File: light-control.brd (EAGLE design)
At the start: 100 x 80 mm, 28 parts, among them IC1 ULN2003AN, IC2 MEGA8-P, K1 JS-M1-12V-5, K2 JS-M1-12V-5, K3 JS-M1-12V-5, K4 JS-M1-12V-5

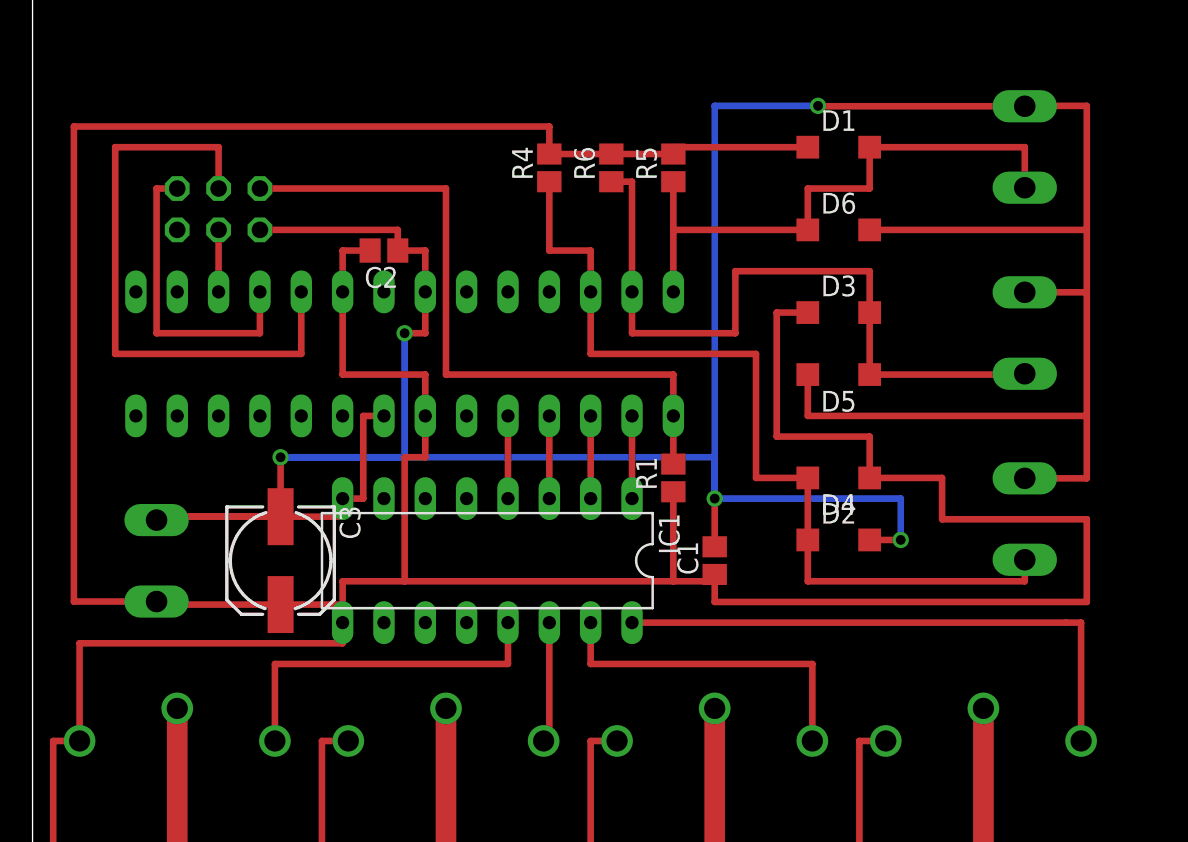
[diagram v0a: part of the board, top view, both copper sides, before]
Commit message: Moved to TQFP
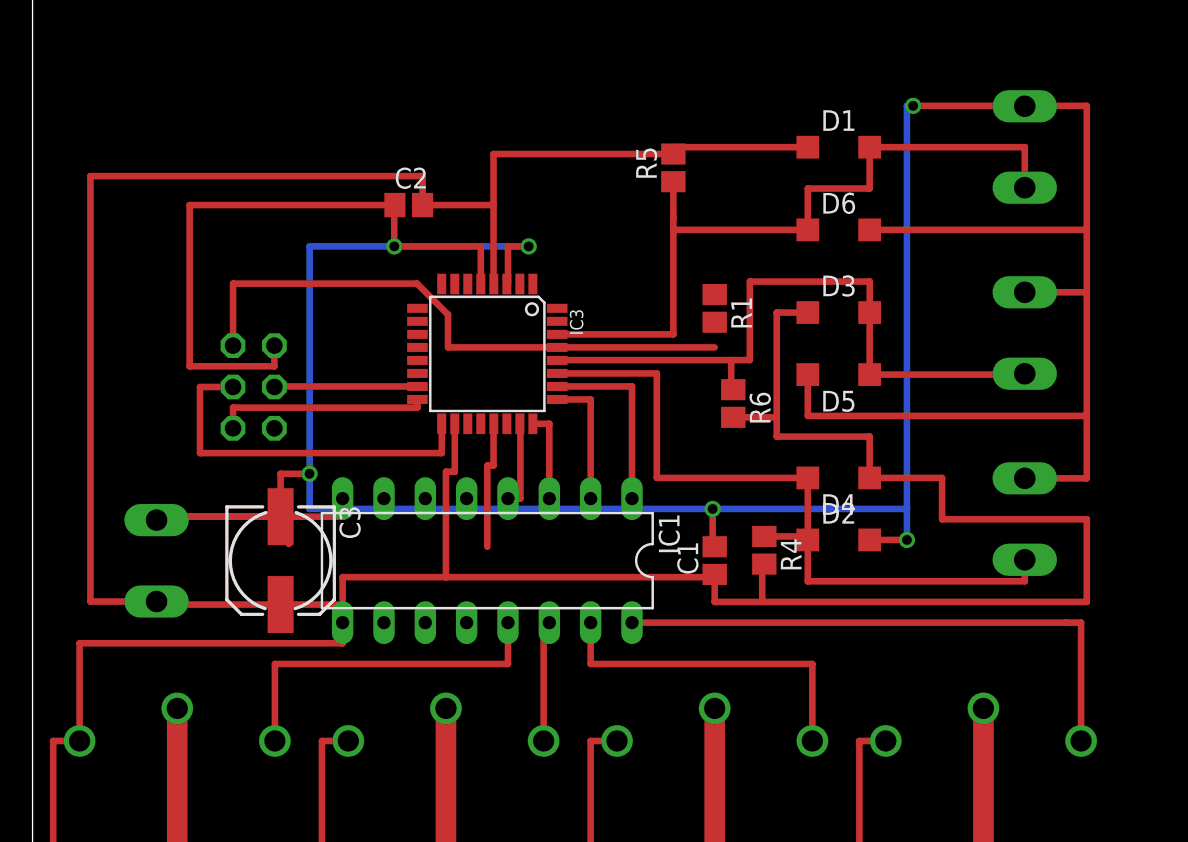
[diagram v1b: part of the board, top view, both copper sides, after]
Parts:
- removed IC2: MEGA8-P, atmel:DIL28-3
- added IC3: MEGA8-AI, atmel:TQFP32-08
- moved R4 27.0 mm to (45.0, 42.5), turned to 270 degrees
- moved R6 16.3 mm to (43.1, 51.6), turned to 270 degrees
- moved JP1 11.1 mm to (13.6, 52.6), turned to 90 degrees
- moved R1 10.7 mm to (41.9, 57.4), turned to 270 degrees
- moved C2 3.18 mm to (23.1, 63.8), turned to 0 degrees
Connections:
- removed net N$1: IC1.1, IC2.2
- removed net N$21: D2.C, D4.A, IC2.26, R4.1, X1.2
- removed net N$22: D3.A, D5.C, IC2.27, R6.1, X2.2
- removed net N$23: D1.A, D6.C, IC2.28, R5.1, X3.2
- removed net N$6: IC1.2, IC2.3
- removed net N$7: IC1.3, IC2.4
- removed net N$8: IC1.4, IC2.5
- new net BUT1: D2.C, D4.A, IC3.27, R4.1, X1.2
- new net BUT2: D3.A, D5.C, IC3.28, R6.1, X2.2
- new net BUT3: D1.A, D6.C, IC3.30, R5.1, X3.2
- new net CHAN1: IC1.1, IC3.26
- new net CHAN2: IC1.2, IC3.25
- new net CHAN3: IC1.3, IC3.24
- new net CHAN4: IC1.4, IC3.23
- new net VCC: IC3.6
- net +5V: now also IC3.18, IC3.4; no longer C1.1, IC2.20, IC2.7
- net GND: now also IC3.21, IC3.3, IC3.5; no longer IC2.22, IC2.8
- net N$2: now also IC3.16; no longer IC2.18
- net N$3: now also IC3.17; no longer IC2.19
- net N$4: now also IC3.15; no longer IC2.17
- net N$5: now also C1.1, IC3.29; no longer IC2.1
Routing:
- net N$21: track 55.1 -> 0.00 mm
- net BUT1: track 0.00 -> 46.0 mm
- net BUT3: track 0.00 -> 45.7 mm
- net N$22: track 44.9 -> 0.00 mm
- net BUT2: track 0.00 -> 41.3 mm
- net N$23: track 35.9 -> 0.00 mm
- net GND: track 222.0 -> 247.5 mm, vias 5 -> 6
- net +5V: track 415.1 -> 399.0 mm
- net N$3: track 36.8 -> 22.8 mm
- net CHAN1: track 0.00 -> 11.5 mm
- net CHAN2: track 0.00 -> 8.15 mm
- net N$5: track 42.3 -> 36.2 mm
- net N$2: track 19.0 -> 13.1 mm
- net CHAN3: track 0.00 -> 5.61 mm
- net CHAN4: track 0.00 -> 5.39 mm
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
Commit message: Some optimizations to board
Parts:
- moved C1 36.0 mm to (7.04, 50.8), turned to 270 degrees
- moved R1 35.7 mm to (6.30, 55.2), turned to 0 degrees
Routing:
- net GND: track 247.5 -> 208.4 mm

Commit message: Some optimizations on board
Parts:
- moved D4 6.47 mm to (43.1, 47.5)
- moved D2 5.34 mm to (53.1, 47.2), turned to 90 degrees
- moved R4 4.42 mm to (40.6, 43.5)
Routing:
- net GND: track 208.4 -> 190.4 mm, vias 6 -> 4
- net BUT1: track 46.0 -> 42.3 mm
- net BUT2: track 41.3 -> 42.3 mm

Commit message: Added initial firmware
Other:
- board size 100 x 80 mm -> 67.6 x 73.8 mm
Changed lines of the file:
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@@
 <?xml version="1.0" encoding="utf-8"?>
 <!DOCTYPE eagle SYSTEM "eagle.dtd">
-<eagle version="7.1.0">
+<eagle version="7.2.0">
 <drawing>
 <settings>
@@
 <setting verticaltext="up"/>
 </settings>
-<grid distance="0.001" unitdist="inch" unit="inch" style="lines" multiple="1" display="no" altdistance="0.0005" altunitdist="inch" altunit="inch"/>
+<grid distance="0.001" unitdist="inch" unit="mm" style="lines" multiple="1" display="no" altdistance="0.0005" altunitdist="inch" altunit="inch"/>
 <layers>
 <layer number="1" name="Top" color="4" fill="1" visible="yes" active="yes"/>
@@
 <layer number="31" name="tCream" color="7" fill="4" visible="no" active="yes"/>
 <layer number="32" name="bCream" color="7" fill="5" visible="no" active="yes"/>
-<layer number="33" name="tFinish" color="6" fill="3" visible="no" active="yes"/>
-<layer number="34" name="bFinish" color="6" fill="6" visible="no" active="yes"/>
+<layer number="33" name="tFinish" color="6" fill="3" visible="yes" active="yes"/>
+<layer number="34" name="bFinish" color="6" fill="6" visible="yes" active="yes"/>
 <layer number="35" name="tGlue" color="7" fill="4" visible="no" active="yes"/>
 <layer number="36" name="bGlue" color="7" fill="5" visible="no" active="yes"/>
-<layer number="37" name="tTest" color="7" fill="1" visible="no" active="yes"/>
-<layer number="38" name="bTest" color="7" fill="1" visible="no" active="yes"/>
+<layer number="37" name="tTest" color="7" fill="1" visible="yes" active="yes"/>
+<layer number="38" name="bTest" color="7" fill="1" visible="yes" active="yes"/>
 <layer number="39" name="tKeepout" color="4" fill="11" visible="yes" active="yes"/>
 <layer number="40" name="bKeepout" color="1" fill="11" visible="yes" active="yes"/>
@@
 <layer number="43" name="vRestrict" color="2" fill="10" visible="yes" active="yes"/>
 <layer number="44" name="Drills" color="7" fill="1" visible="no" active="yes"/>
-<layer number="45" name="Holes" color="7" fill="1" visible="no" active="yes"/>
-<layer number="46" name="Milling" color="3" fill="1" visible="no" active="yes"/>
-<layer number="47" name="Measures" color="7" fill="1" visible="no" active="yes"/>
+<layer number="45" name="Holes" color="7" fill="1" visible="yes" active="yes"/>
+<layer number="46" name="Milling" color="3" fill="1" visible="yes" active="yes"/>
+<layer number="47" name="Measures" color="7" fill="1" visible="yes" active="yes"/>
 <layer number="48" name="Document" color="7" fill="1" visible="yes" active="yes"/>
 <layer number="49" name="Reference" color="7" fill="1" visible="yes" active="yes"/>
@@
 <layer number="98" name="Guide" color="6" fill="1" visible="no" active="no"/>
 <layer number="99" name="SpiceOrder" color="5" fill="1" visible="no" active="no"/>
+<layer number="116" name="centerDrill" color="7" fill="1" visible="no" active="yes"/>
 </layers>
 <board>
 <plain>
-<wire x1="0" y1="0" x2="100" y2="0" width="0" layer="20"/>
-<wire x1="100" y1="0" x2="100" y2="80" width="0" layer="20"/>
-<wire x1="100" y1="80" x2="0" y2="80" width="0" layer="20"/>
-<wire x1="0" y1="80" x2="0" y2="0" width="0" layer="20"/>
+<wire x1="0" y1="0" x2="67.6404" y2="0" width="0" layer="20"/>
+<wire x1="67.6404" y1="0" x2="67.6404" y2="73.777" width="0" layer="20"/>
+<wire x1="67.6404" y1="73.777" x2="0" y2="73.777" width="0" layer="20"/>
+<wire x1="0" y1="73.777" x2="0" y2="0" width="0" layer="20"/>
+<circle x="36.83" y="45.72" radius="0.303" width="0.306" layer="116"/>
+<circle x="34.29" y="45.72" radius="0.303" width="0.306" layer="116"/>
+<circle x="31.75" y="45.72" radius="0.303" width="0.306" layer="116"/>
+<circle x="29.21" y="45.72" radius="0.303" width="0.306" layer="116"/>
+<circle x="26.67" y="45.72" radius="0.303" width="0.306" layer="116"/>
+<circle x="24.13" y="45.72" radius="0.303" width="0.306" layer="116"/>
+<circle x="21.59" y="45.72" radius="0.303" width="0.306" layer="116"/>
+<circle x="19.05" y="45.72" radius="0.303" width="0.306" layer="116"/>
+<circle x="19.05" y="38.1" radius="0.303" width="0.306" layer="116"/>
+<circle x="21.59" y="38.1" radius="0.303" width="0.306" layer="116"/>
+<circle x="24.13" y="38.1" radius="0.303" width="0.306" layer="116"/>
+<circle x="26.67" y="38.1" radius="0.303" width="0.306" layer="116"/>
+<circle x="29.21" y="38.1" radius="0.303" width="0.306" layer="116"/>
+<circle x="31.75" y="38.1" radius="0.303" width="0.306" layer="116"/>
+<circle x="34.29" y="38.1" radius="0.303" width="0.306" layer="116"/>
+<circle x="36.83" y="38.1" radius="0.303" width="0.306" layer="116"/>
+<circle x="12.319" y="50.038" radius="0.354" width="0.408" layer="116"/>
+<circle x="14.859" y="50.038" radius="0.354" width="0.408" layer="116"/>
+<circle x="12.319" y="52.578" radius="0.354" width="0.408" layer="116"/>
+<circle x="14.859" y="52.578" radius="0.354" width="0.408" layer="116"/>
+<circle x="12.319" y="55.118" radius="0.354" width="0.408" layer="116"/>
+<circle x="14.859" y="55.118" radius="0.354" width="0.408" layer="116"/>
+<circle x="64.42" y="30.83" radius="0.425" width="0.55" layer="116"/>
+<circle x="52.42" y="30.83" radius="0.425" width="0.55" layer="116"/>
+<circle x="58.42" y="32.83" radius="0.425" width="0.55" layer="116"/>
+<circle x="52.42" y="18.63" radius="0.425" width="0.55" layer="116"/>
+<circle x="64.42" y="18.63" radius="0.425" width="0.55" layer="116"/>
+<circle x="47.91" y="30.83" radius="0.425" width="0.55" layer="116"/>
+<circle x="35.91" y="30.83" radius="0.425" width="0.55" layer="116"/>
+<circle x="41.91" y="32.83" radius="0.425" width="0.55" layer="116"/>
+<circle x="35.91" y="18.63" radius="0.425" width="0.55" layer="116"/>
+<circle x="47.91" y="18.63" radius="0.425" width="0.55" layer="116"/>
+<circle x="31.4" y="30.83" radius="0.425" width="0.55" layer="116"/>
+<circle x="19.4" y="30.83" radius="0.425" width="0.55" layer="116"/>
+<circle x="25.4" y="32.83" radius="0.425" width="0.55" layer="116"/>
+<circle x="19.4" y="18.63" radius="0.425" width="0.55" layer="116"/>
+<circle x="31.4" y="18.63" radius="0.425" width="0.55" layer="116"/>
+<circle x="14.89" y="30.83" radius="0.425" width="0.55" layer="116"/>
+<circle x="2.89" y="30.83" radius="0.425" width="0.55" layer="116"/>
+<circle x="8.89" y="32.83" radius="0.425" width="0.55" layer="116"/>
+<circle x="2.89" y="18.63" radius="0.425" width="0.55" layer="116"/>
+<circle x="14.89" y="18.63" radius="0.425" width="0.55" layer="116"/>
+<circle x="7.62" y="39.395" radius="0.43" width="0.56" layer="116"/>
+<circle x="7.62" y="44.399" radius="0.43" width="0.56" layer="116"/>
+<circle x="60.96" y="46.965" radius="0.43" width="0.56" layer="116"/>
+<circle x="60.96" y="41.961" radius="0.43" width="0.56" layer="116"/>
+<circle x="60.96" y="58.395" radius="0.43" width="0.56" layer="116"/>
+<circle x="60.96" y="53.391" radius="0.43" width="0.56" layer="116"/>
+<circle x="60.96" y="69.825" radius="0.43" width="0.56" layer="116"/>
+<circle x="60.96" y="64.821" radius="0.43" width="0.56" layer="116"/>
+<circle x="63.424" y="6.35" radius="0.43" width="0.56" layer="116"/>
+<circle x="58.42" y="6.35" radius="0.43" width="0.56" layer="116"/>
+<circle x="53.416" y="6.35" radius="0.43" width="0.56" layer="116"/>
+<circle x="46.914" y="6.35" radius="0.43" width="0.56" layer="116"/>
+<circle x="41.91" y="6.35" radius="0.43" width="0.56" layer="116"/>
+<circle x="36.906" y="6.35" radius="0.43" width="0.56" layer="116"/>
+<circle x="30.404" y="6.35" radius="0.43" width="0.56" layer="116"/>
+<circle x="25.4" y="6.35" radius="0.43" width="0.56" layer="116"/>
+<circle x="20.396" y="6.35" radius="0.43" width="0.56" layer="116"/>
+<circle x="15.164" y="6.35" radius="0.43" width="0.56" layer="116"/>
+<circle x="10.16" y="6.35" radius="0.43" width="0.56" layer="116"/>
+<circle x="5.156" y="6.35" radius="0.43" width="0.56" layer="116"/>
+<circle x="28.346" y="48.057" radius="0.25" width="0.2" layer="116"/>
+<circle x="17.145" y="46.939" radius="0.25" width="0.2" layer="116"/>
+<circle x="31.191" y="61.849" radius="0.25" width="0.2" layer="116"/>
+<circle x="47.65" y="48.997" radius="0.25" width="0.2" layer="116"/>
 </plain>
 <attributes>

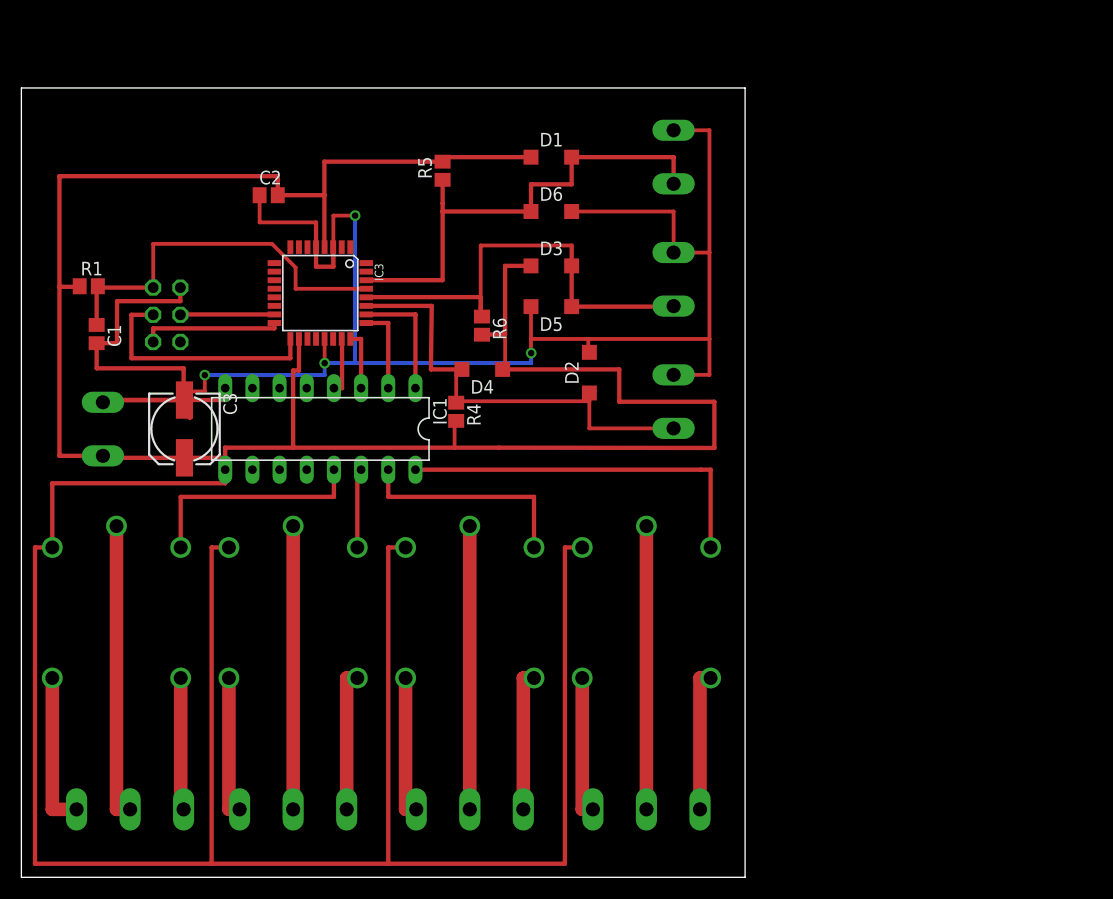
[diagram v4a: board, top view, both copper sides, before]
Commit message: Fixed schematic
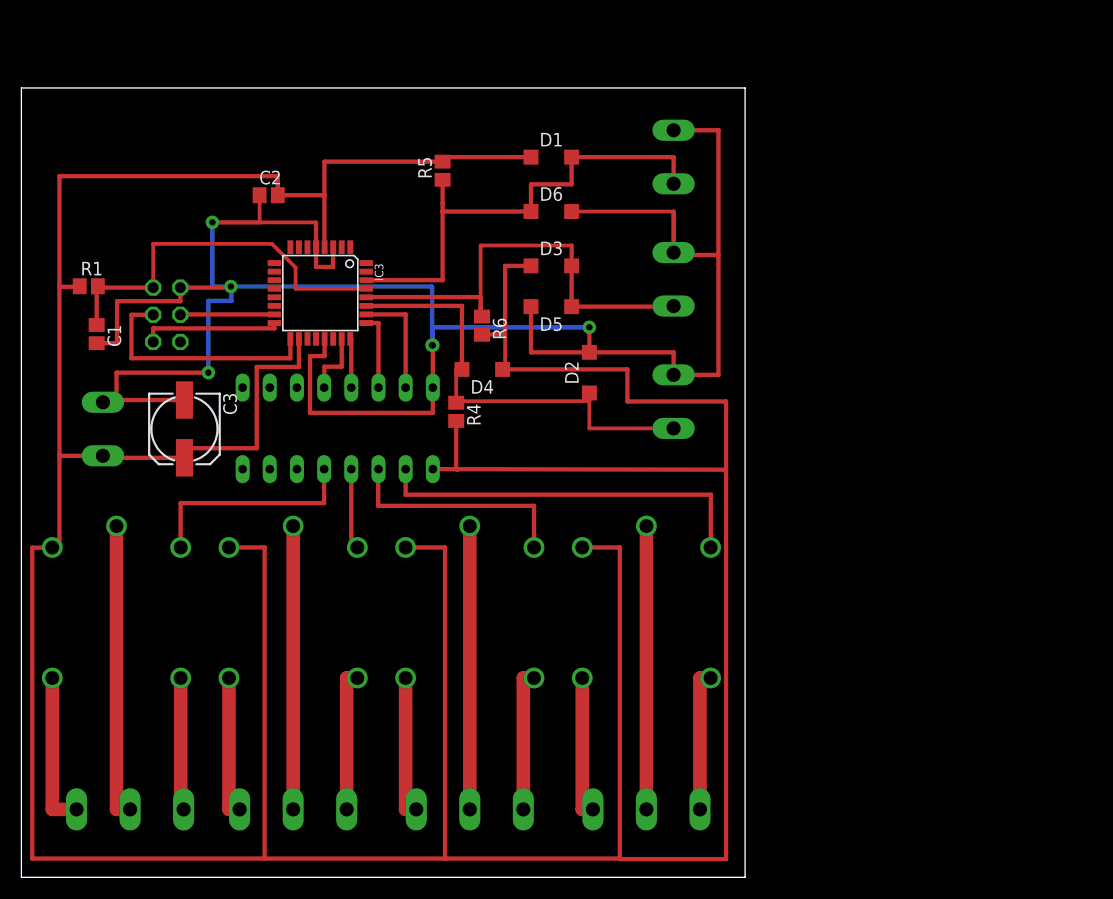
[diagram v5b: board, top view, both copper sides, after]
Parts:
- moved IC1 1.63 mm to (29.6, 42.0), flipped to the bottom
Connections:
- removed net N$12 (its old number): IC1.14, K3.1
- new net N$1: IC1.1
- new net N$6: IC1.2
- new net N$7: IC1.3
- new net N$8: IC1.10, K1.1
- net CHAN1: now also IC1.4, IC3.23; no longer IC1.1, IC3.26
- net CHAN2: now also IC1.5, IC3.24; no longer IC1.2, IC3.25
- net CHAN3: now also IC1.6, IC3.25; no longer IC1.3, IC3.24
- net CHAN4: now also IC1.7, IC3.26; no longer IC1.4, IC3.23
- net N$10: now also IC1.11, K2.1; no longer IC1.16, K1.1
- net N$11: now also IC1.12, K3.1; no longer IC1.15, K2.1
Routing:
- net N$8: track 0.00 -> 35.9 mm
- net +5V: track 399.7 -> 433.0 mm
- net GND: track 190.4 -> 216.3 mm, vias 4 -> 6
- net N$11: track 20.9 -> 7.89 mm
- net N$10: track 34.9 -> 21.9 mm
- net N$12 (its old number): track 7.62 -> 0.00 mm
- net CHAN1: track 11.5 -> 6.19 mm
- net CHAN4: track 5.39 -> 10.5 mm
- net CHAN2: track 8.15 -> 4.64 mm
- net CHAN3: track 5.61 -> 7.18 mm
- net N$12: track 21.6 -> 20.7 mm
